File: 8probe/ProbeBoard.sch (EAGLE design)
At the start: 60 parts, among them Q1 2N7002, Q2 2N7002, U1 LTC2495CUHFPBF, U3 MAX6037AAUKADJ+T, U4 CSTCE16M0V53A-R0, U5 TPS79733DCKR, U6 ATMEGA328P_TQFPQFN_32

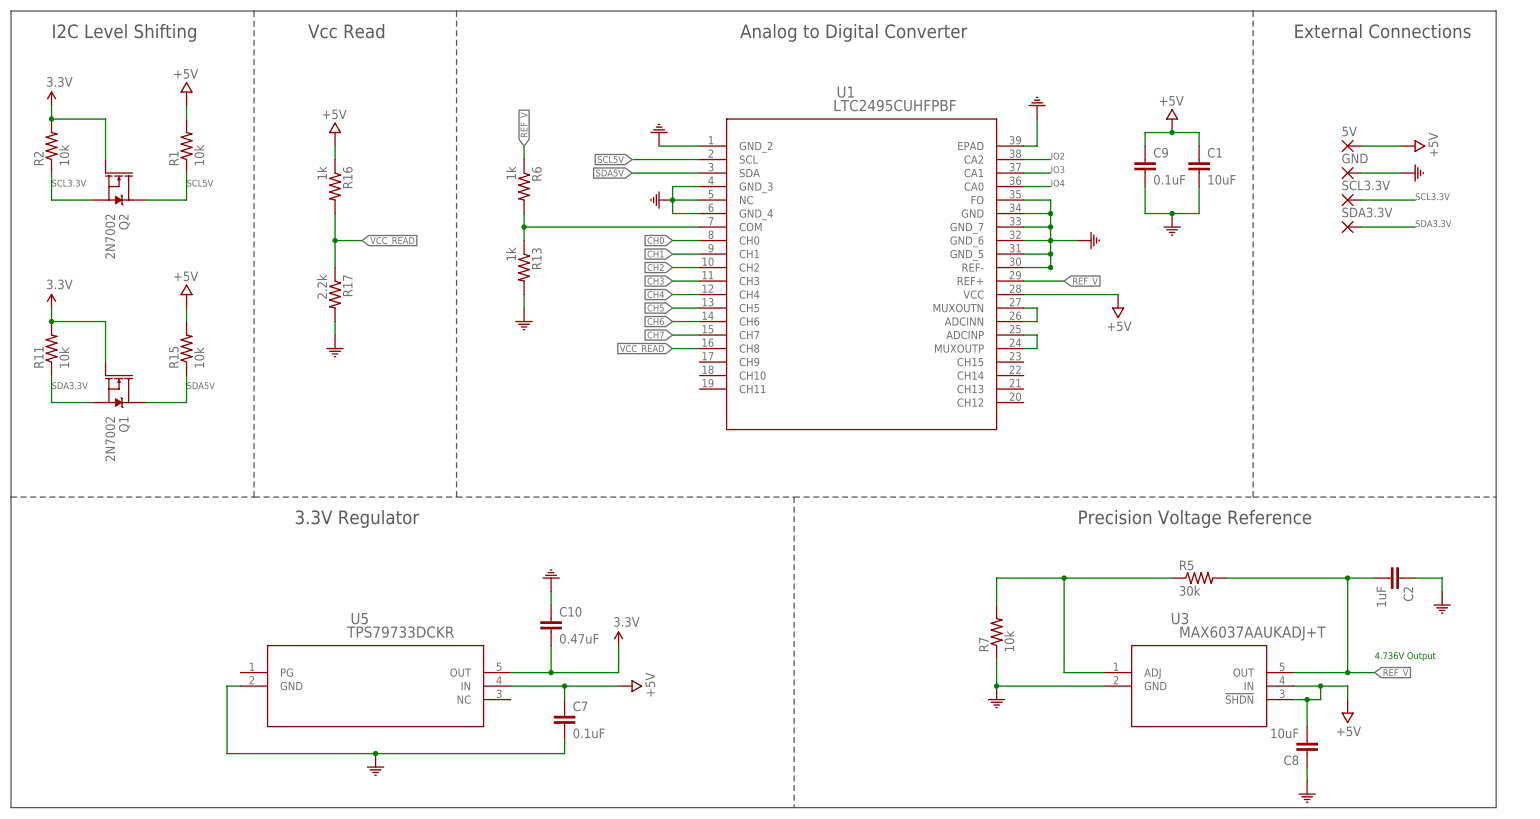
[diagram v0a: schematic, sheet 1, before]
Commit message: Updates to 8probe layout, 8probe v0.1 to fab
Minor updates and cleanup to 8probe layout, generated gerbers for 8probe v0.1 sent to fab
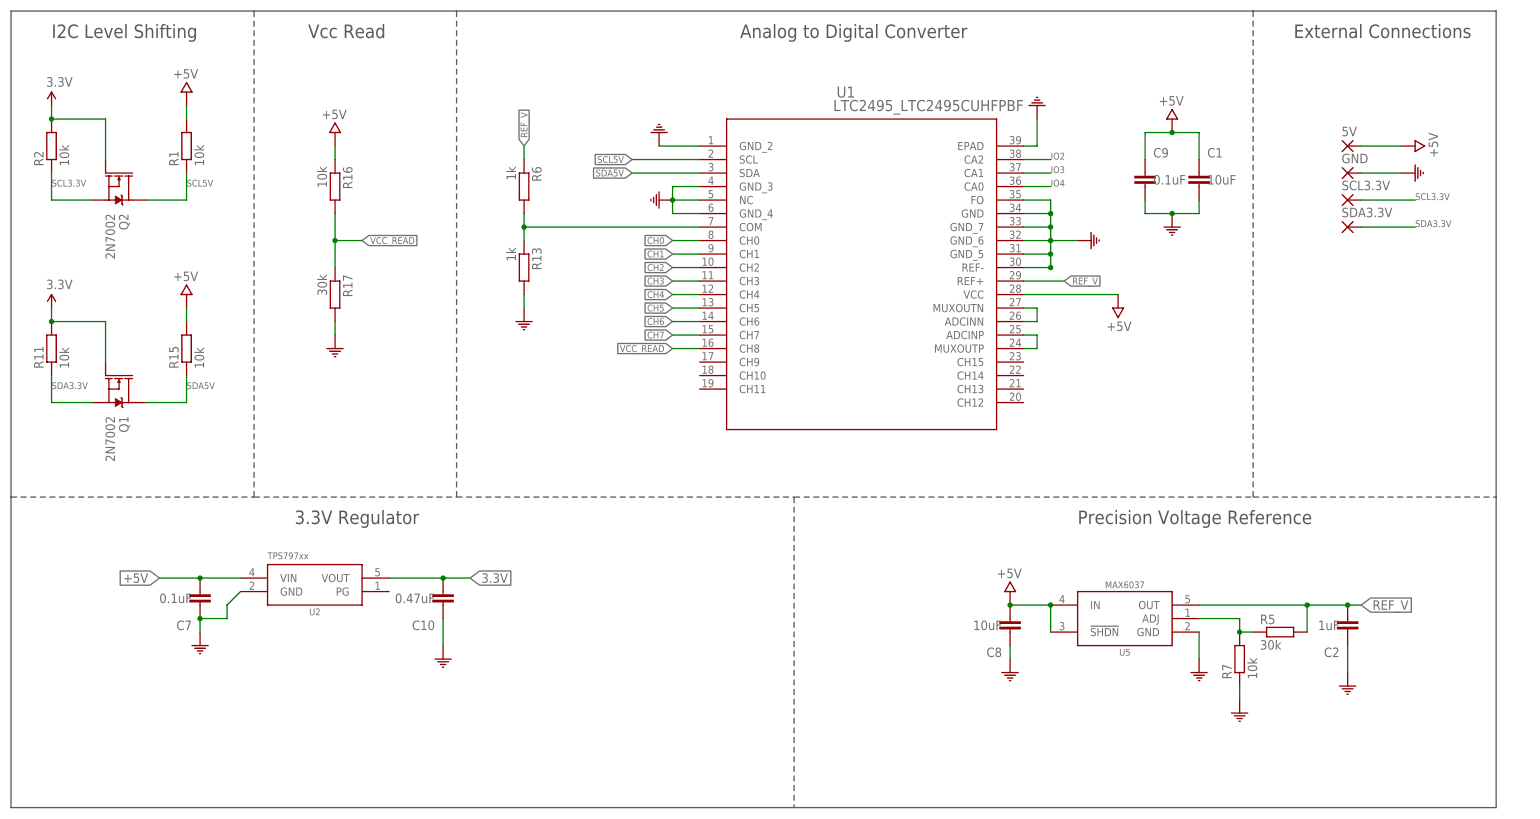
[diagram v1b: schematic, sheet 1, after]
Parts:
- removed U3: MAX6037AAUKADJ+T, MAX6037AAUKADJ:MAX6037AAUKADJ+T
- removed U4: CSTCE16M0V53A-R0, Murata Resonator:CSTCE16M0V53A-R0
- added U2: TPS79733, bschulz:TPS79733
- added Y1: 16MHz, bschulz:RESONATOR16MHZSMD_3.2X1.3
- C1, C8: device SparkFun:CAP0603-CAP -> bschulz_passives:C-EU10UFC0603
- C10: device SparkFun:CAP0603-CAP -> bschulz_passives:C-EU0.47UFC0603
- C2: device SparkFun:CAP0603-CAP -> bschulz_passives:C-EU1UFC0603
- C3, C5, C7, C9: device SparkFun:CAP0603-CAP -> bschulz_passives:C-EU0.1UFC0603
- R1, R11, R14, R15, R2: device SparkFun:RESISTOR0603-RES -> bschulz_passives:R-EU_10KR0603
- R10, R12, R19, R20, R3, R4, R8, R9: device SparkFun:RESISTOR0603-RES -> bschulz_passives:R-EU_R0603
- R13, R6: device SparkFun:RESISTOR0603-RES -> bschulz_passives:R-EU_P1KR0603
- R16: value 1k -> 10k; device SparkFun:RESISTOR0603-RES -> bschulz_passives:R-EU_P10KR0603
- R17: value 2.2k -> 30k; device SparkFun:RESISTOR0603-RES -> bschulz_passives:R-EU_P30KR0603
- R5: device SparkFun:RESISTOR0603-RES -> bschulz_passives:R-EU_P30KR0603
- R7: device SparkFun:RESISTOR0603-RES -> bschulz_passives:R-EU_P10KR0603
- U1: value LTC2495CUHFPBF -> LTC2495_LTC2495CUHFPBF; device LTC2495:LTC2495CUHFPBF -> ProbeBoard:LTC2495_LTC2495CUHFPBF
- U5: value TPS79733DCKR -> MAX6037ADJSOT23; device TPS79733:TPS79733DCKR -> bschulz:MAX6037ADJSOT23; DIGIKEY_PART_NUMBER 296-11990-6-ND -> (none); MANUFACTURER Texas Instruments -> (none); PRICE 0.46196 -> (none)
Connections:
- removed net N$6: R5.1, R7.2, U3.ADJ
- new net N$4: R5.1, R7.2, U5.ADJ
- net +5V: now also C7.2, U2.VIN, U5.!SHDN; no longer C7.1, U3.!SHDN, U3.IN
- net 3.3V: now also U2.VOUT; no longer U5.OUT
- net COM: now also C7.1, U2.GND, Y1.2; no longer C7.2, U3.GND, U4.2
- net N$1: now also Y1.3; no longer U4.3
- net N$7: now also Y1.1; no longer U4.1
- net REF_V: now also U5.OUT; no longer U3.OUT
- net SCL5V: now also U6.PC5(ADC5/SCL)
- net SDA5V: now also U6.PC4(ADC4/SDA)
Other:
- note removed: "4.736V Output"
- moved on the sheet: C1, C10, C2, C3, C5, C7, C8, C9
